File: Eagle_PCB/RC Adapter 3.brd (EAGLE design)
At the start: 50.8 x 35.6 mm, 21 parts, among them IC1 DRV8833, IC2 DRV8833, IC3 ARDUINO_PRO_MICRO, X1 MKDSN1,5/2-5,08

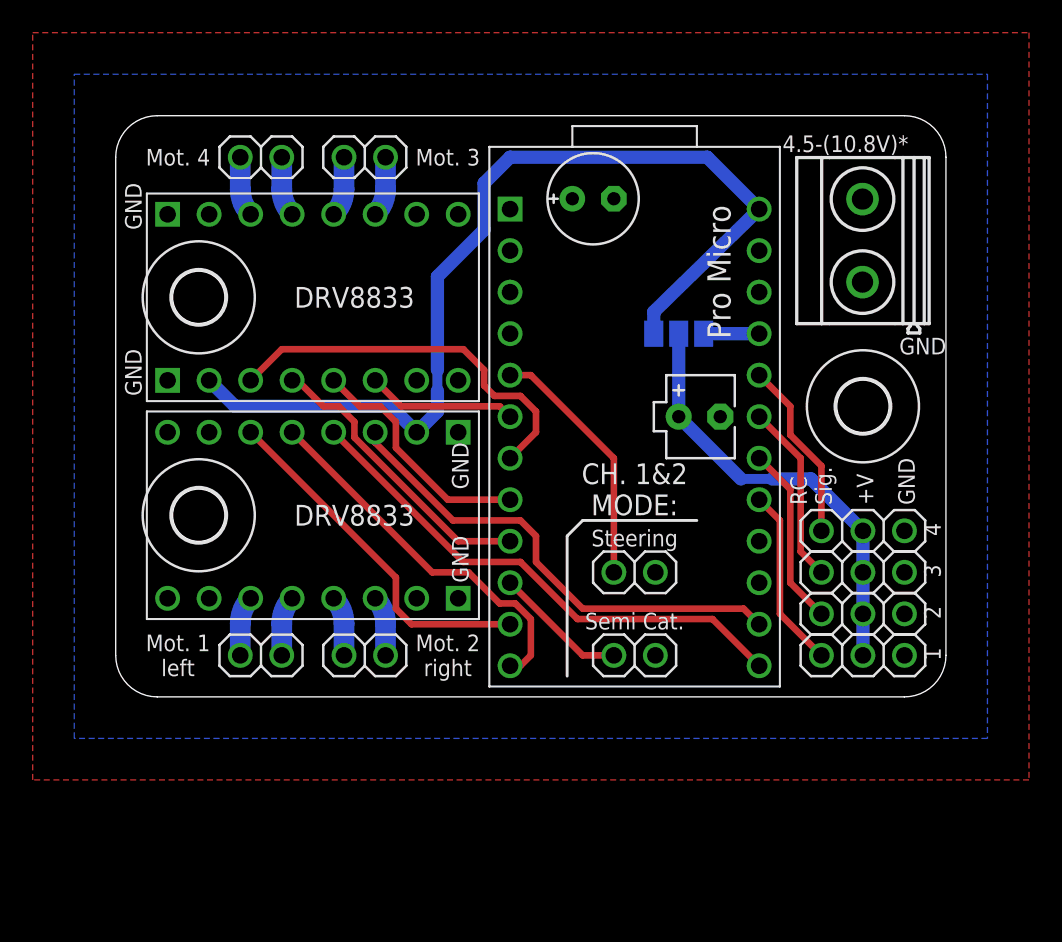
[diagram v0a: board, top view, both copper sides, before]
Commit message: Updated to V1.1
Now also compatible with a Pro Mini
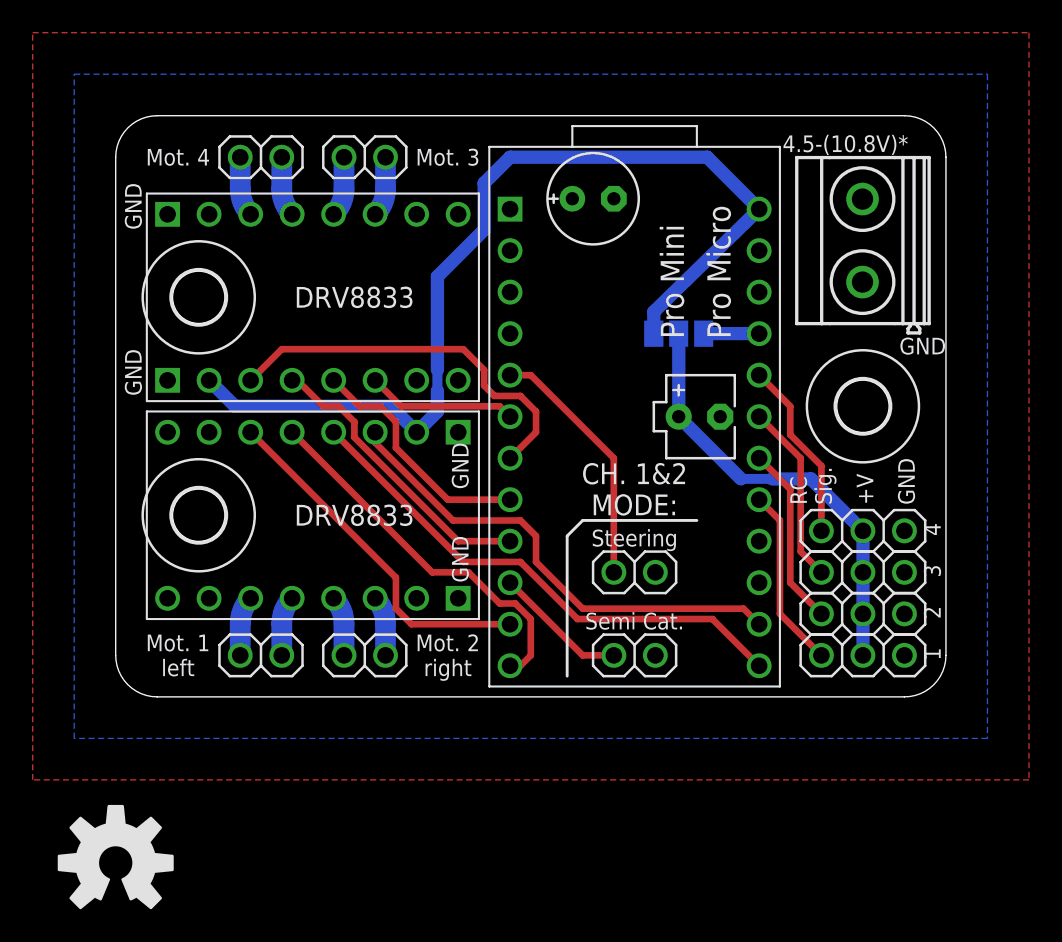
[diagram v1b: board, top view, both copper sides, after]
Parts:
- added LOGO1: OSHW-LOGOL, SparkFun-Aesthetics:OSHW-LOGO-L
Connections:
- net GND: no longer IC3.3
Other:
- board text added: "4 Channel RC to DC Motor Shield V1.1"
- board text added: "Pro Mini"
- board text removed: "4 Channel RC to DC Motor Shield"
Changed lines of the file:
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@@
 <text x="3.81" y="33.02" size="1.016" layer="25" align="center">Mot. 4
 </text>
-<text x="25.4" y="3.96875" size="1.016" layer="26" rot="MR90">4 Channel RC to DC Motor Shield</text>
+<text x="25.4" y="17.78" size="1.016" layer="26" rot="MR90" align="bottom-center">4 Channel RC to DC Motor Shield V1.1</text>
 <text x="33.9725" y="25.0825" size="1.016" layer="26" rot="MR0" align="center">Rec. Sup. *
 Reg. / Bat.</text>
@@
 = 400mA</text>
 <text x="37.62375" y="21.9075" size="1.4224" layer="25" rot="R90">Pro Micro</text>
+<text x="34.76625" y="21.9075" size="1.4224" layer="25" rot="R90">Pro Mini</text>
 </plain>
 <attributes>
@@
 </element>
 <element name="C2" library="rcl" package="ETR1" value="3.3uF 16V" x="35.71875" y="17.145" smashed="yes"/>
+<element name="LOGO1" library="SparkFun-Aesthetics" package="OSHW-LOGO-L" value="OSHW-LOGOL" x="0" y="-10.16"/>
 </elements>
 <signals>
@@
 <vertex x="-2.54" y="-2.54"/>
 </polygon>
-<contactref element="IC3" pad="3"/>
 <contactref element="IC3" pad="4"/>
 <contactref element="IC3" pad="23"/>
